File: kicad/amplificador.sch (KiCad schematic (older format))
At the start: 77 parts, among them J1 Screw_Terminal_01x01, J10 Conn_01x01_Male, J11 Conn_01x01_Male, J12 Conn_01x01_Male, J13 Conn_01x01_Male, J14 Conn_01x01_Male, J15 Conn_01x01_Male, J16 Screw_Terminal_01x01, J17 Screw_Terminal_01x01, J18 Conn_01x01_Male, J2 Conn_01x01_Male, J3 Conn_01x01_Male, J4 Conn_01x01_Male, J5 Conn_01x01_Male, J6 Conn_01x01_Male, J7 Screw_Terminal_01x01, J8 Screw_Terminal_01x01, J9 Conn_01x01_Male, Q1 MPSA92, Q10 MPSA42, Q11 BD135, Q12 BD136, Q13 BD135, Q14 BD136, Q15 2SD1047, Q16 2SD1047, Q17 2SB817, Q18 2SB817, Q2 MPSA42, Q3 MPSA92, Q4 MPSA42, Q5 MPSA92, Q6 MPSA92, Q7 MPSA42, Q8 MPSA92, Q9 MPSA42, U1 LM385D-1.2, U2 LM385D-1.2

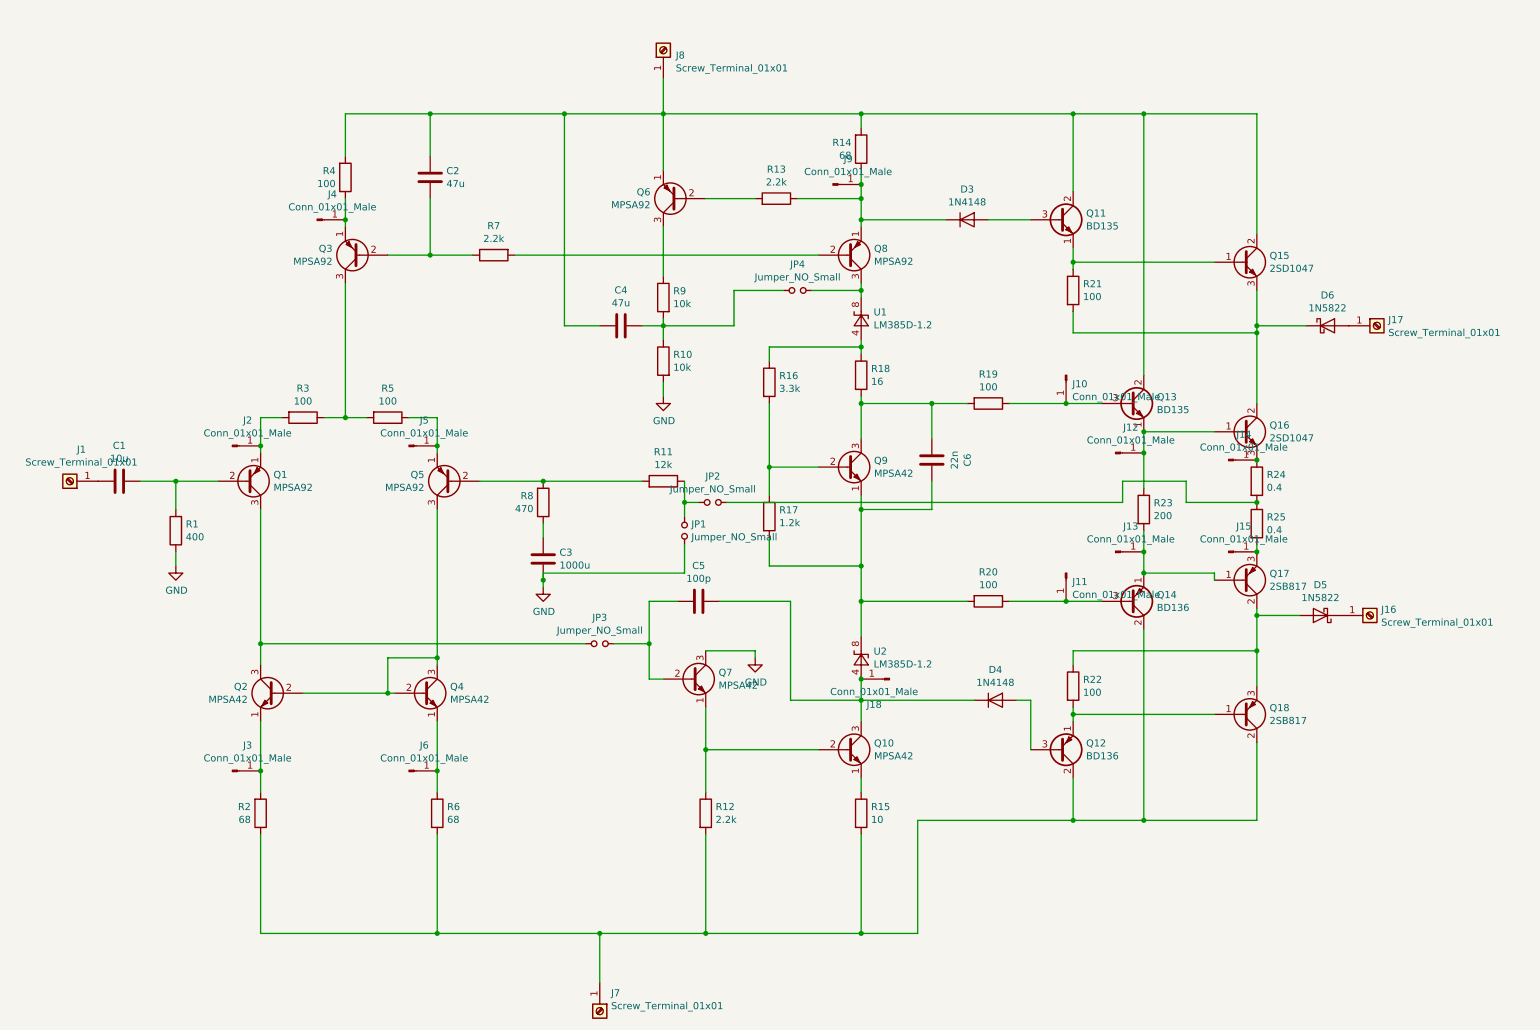
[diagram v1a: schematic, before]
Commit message: agregamos hojas de datos, cambiamos el esquematico un poco (footprints, sacamos algunos pines, agregamos capas de filtrado), el pcb esta dispuesto de la misma forma que el esquematico, queda optimizarlo y rutear
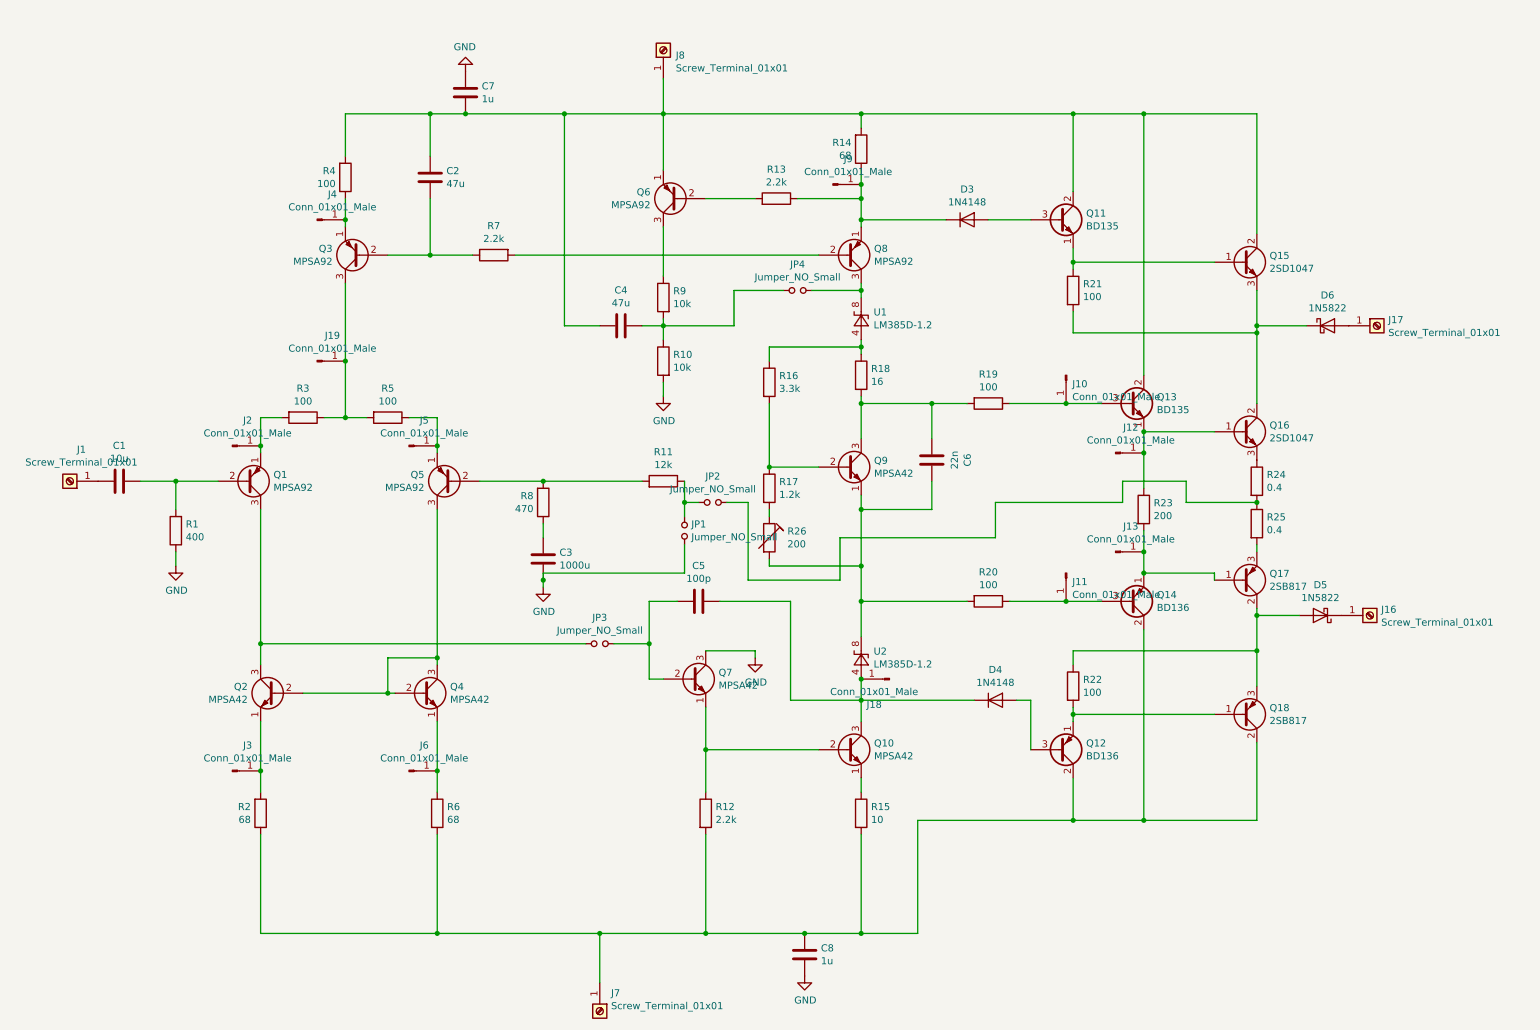
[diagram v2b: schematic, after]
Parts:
- removed J14, J15: Conn_01x01_Male, Connector_Pin:Pin_D0.7mm_L6.5mm_W1.8mm_FlatFork, symbol Connector:Conn_01x01_Male
- added C7, C8: 1u, Capacitor_THT:CP_Radial_D5.0mm_P2.00mm, symbol Device:C
- added J19: Conn_01x01_Male, Connector_Pin:Pin_D0.7mm_L6.5mm_W1.8mm_FlatFork, symbol Connector:Conn_01x01_Male
- added R26: 200, Resistor_THT:R_Box_L8.4mm_W2.5mm_P5.08mm, symbol Device:RTRIM
- R24, R25: footprint Resistor_SMD:R_0805_2012Metric_Pad1.15x1.40mm_HandSolder -> Resistor_THT:R_Axial_DIN0414_L11.9mm_D4.5mm_P25.40mm_Horizontal
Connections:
- net GND: now also C7.1, C8.2
- net at Q3.3 (C), R3.1, R5.2: now also J19.1 (Pin_1)
- net at J7.1 (Pin_1), Q12.2 (C), Q14.2 (C)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: now also C8.1
- net at C2.2, C4.2, J8.1 (Pin_1)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: now also C7.2
- net at C6.1, Q9.1 (E), R20.2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: now also R26.2; no longer R17.2
- new net: R17.2, R26.1
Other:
- moved on the sheet: R17
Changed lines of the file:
@@
 Connection ~ 5350 7050
 Wire Wire Line
-	5350 7050 6450 7050
+	5350 7050 6050 7050
 Wire Wire Line
 	3450 4050 3450 5100
@@
 	5050 2750 5050 2700
 Wire Wire Line
-	2800 2450 2800 3400
+	2800 2450 2800 3000
 Connection ~ 2800 3400
 Wire Wire Line
@@
 	5050 1000 5050 1250
 Wire Wire Line
-	3400 1250 4350 1250
+	3400 1250 3650 1250
 Wire Wire Line
 	4600 2750 4350 2750
@@
 L Device:R R17
 U 1 1 5D084E8F
-P 5800 4100
-F 0 "R17" H 5870 4146 50  0000 L CNN
-F 1 "1.2k" H 5870 4055 50  0000 L CNN
-F 2 "Resistor_SMD:R_0805_2012Metric_Pad1.15x1.40mm_HandSolder" V 5730 4100 50  0001 C CNN
-F 3 "~" H 5800 4100 50  0001 C CNN
-	1    5800 4100
+P 5800 3900
+F 0 "R17" H 5870 3946 50  0000 L CNN
+F 1 "1.2k" H 5870 3855 50  0000 L CNN
+F 2 "Resistor_SMD:R_0805_2012Metric_Pad1.15x1.40mm_HandSolder" V 5730 3900 50  0001 C CNN
+F 3 "~" H 5800 3900 50  0001 C CNN
+	1    5800 3900
 	1    0    0    -1
 $EndComp
@@
 Wire Wire Line
 	5800 2900 5800 3000
-Wire Wire Line
-	5800 3300 5800 3750
 Connection ~ 5800 3750
-Wire Wire Line
-	5800 3750 5800 3950
-Wire Wire Line
-	5800 4250 5800 4450
 Wire Wire Line
 	5800 4450 6450 4450
@@
 F 0 "R25" H 9320 4196 50  0000 L CNN
 F 1 "0.4" H 9320 4105 50  0000 L CNN
-F 2 "Resistor_SMD:R_0805_2012Metric_Pad1.15x1.40mm_HandSolder" V 9180 4150 50  0001 C CNN
+F 2 "Resistor_THT:R_Axial_DIN0414_L11.9mm_D4.5mm_P25.40mm_Horizontal" V 9180 4150 50  0001 C CNN
 F 3 "~" H 9250 4150 50  0001 C CNN
 	1    9250 4150
@@
 F 0 "R24" H 9320 3896 50  0000 L CNN
 F 1 "0.4" H 9320 3805 50  0000 L CNN
-F 2 "Resistor_SMD:R_0805_2012Metric_Pad1.15x1.40mm_HandSolder" V 9180 3850 50  0001 C CNN
+F 2 "Resistor_THT:R_Axial_DIN0414_L11.9mm_D4.5mm_P25.40mm_Horizontal" V 9180 3850 50  0001 C CNN
 F 3 "~" H 9250 3850 50  0001 C CNN
 	1    9250 3850
@@
 Wire Wire Line
 	8750 4000 9250 4000
-Wire Wire Line
-	5500 4000 8300 4000
 Connection ~ 9250 4000
 Wire Wire Line
@@
 	6450 1750 6450 1850
 $Comp
-L Connector:Conn_01x01_Male J14
-U 1 1 5D20277F
-P 9050 3700
-F 0 "J14" H 9158 3881 50  0000 C CNN
-F 1 "Conn_01x01_Male" H 9158 3790 50  0000 C CNN
-F 2 "Connector_Pin:Pin_D0.7mm_L6.5mm_W1.8mm_FlatFork" H 9050 3700 50  0001 C CNN
-F 3 "~" H 9050 3700 50  0001 C CNN
-	1    9050 3700
-	1    0    0    -1
-$EndComp
-Connection ~ 9250 3700
-$Comp
-L Connector:Conn_01x01_Male J15
-U 1 1 5D20324F
-P 9050 4350
-F 0 "J15" H 9158 4531 50  0000 C CNN
-F 1 "Conn_01x01_Male" H 9158 4440 50  0000 C CNN
-F 2 "Connector_Pin:Pin_D0.7mm_L6.5mm_W1.8mm_FlatFork" H 9050 4350 50  0001 C CNN
-F 3 "~" H 9050 4350 50  0001 C CNN
-	1    9050 4350
-	1    0    0    -1
-$EndComp
-$Comp
 L Connector:Conn_01x01_Male J10
 U 1 1 5D20366F
@@
 Wire Wire Line
 	9250 4350 9250 4300
-Connection ~ 9250 4350
 Wire Wire Line
 	5950 5400 6450 5400
@@
 Wire Wire Line
 	5550 2750 5050 2750
+$Comp
+L Connector:Conn_01x01_Male J19
+U 1 1 5D204C85
+P 2600 3000
+F 0 "J19" H 2708 3181 50  0000 C CNN
+F 1 "Conn_01x01_Male" H 2708 3090 50  0000 C CNN
+F 2 "Connector_Pin:Pin_D0.7mm_L6.5mm_W1.8mm_FlatFork" H 2600 3000 50  0001 C CNN
+F 3 "~" H 2600 3000 50  0001 C CNN
+	1    2600 3000
+	1    0    0    -1
+$EndComp
+Connection ~ 2800 3000
+Wire Wire Line
+	2800 3000 2800 3400
+Wire Wire Line
+	5800 4050 5800 4100
+Wire Wire Line
+	5800 3300 5800 3750
+Wire Wire Line
+	5800 4400 5800 4450
+$Comp
+L Device:RTRIM R26
+U 1 1 5D251E27
+P 5800 4250
+F 0 "R26" H 5928 4296 50  0000 L CNN
+F 1 "200" H 5928 4205 50  0000 L CNN
+F 2 "Resistor_THT:R_Box_L8.4mm_W2.5mm_P5.08mm" V 5730 4250 50  0001 C CNN
+F 3 "~" H 5800 4250 50  0001 C CNN
+	1    5800 4250
+	1    0    0    -1
+$EndComp
+Wire Wire Line
+	8300 4000 7400 4000
+Wire Wire Line
+	7400 4000 7400 4250
+Wire Wire Line
+	7400 4250 6300 4250
+Wire Wire Line
+	6300 4250 6300 4550
+Wire Wire Line
+	6300 4550 5650 4550
+Wire Wire Line
+	5650 4550 5650 4000
+Wire Wire Line
+	5650 4000 5500 4000
+$Comp
+L Device:C C8
+U 1 1 5D2CF0A1
+P 6050 7200
+F 0 "C8" H 6165 7246 50  0000 L CNN
+F 1 "1u" H 6165 7155 50  0000 L CNN
+F 2 "Capacitor_THT:CP_Radial_D5.0mm_P2.00mm" H 6088 7050 50  0001 C CNN
+F 3 "~" H 6050 7200 50  0001 C CNN
+	1    6050 7200
+	1    0    0    -1
+$EndComp
+Connection ~ 6050 7050
+Wire Wire Line
+	6050 7050 6450 7050
+$Comp
+L power:GND #PWR04
+U 1 1 5D2CFEDE
+P 6050 7350
+F 0 "#PWR04" H 6050 7100 50  0001 C CNN
+F 1 "GND" H 6055 7177 50  0000 C CNN
+F 2 "" H 6050 7350 50  0001 C CNN
+F 3 "" H 6050 7350 50  0001 C CNN
+	1    6050 7350
+	1    0    0    -1
+$EndComp
+$Comp
+L Device:C C7
+U 1 1 5D2D03B4
+P 3650 1100
+F 0 "C7" H 3765 1146 50  0000 L CNN
+F 1 "1u" H 3765 1055 50  0000 L CNN
+F 2 "Capacitor_THT:CP_Radial_D5.0mm_P2.00mm" H 3688 950 50  0001 C CNN
+F 3 "~" H 3650 1100 50  0001 C CNN
+	1    3650 1100
+	1    0    0    -1
+$EndComp
+Connection ~ 3650 1250
+Wire Wire Line
+	3650 1250 4350 1250
+$Comp
+L power:GND #PWR03
+U 1 1 5D2D9DE0
+P 3650 950
+F 0 "#PWR03" H 3650 700 50  0001 C CNN
+F 1 "GND" H 3655 777 50  0000 C CNN
+F 2 "" H 3650 950 50  0001 C CNN
+F 3 "" H 3650 950 50  0001 C CNN
+	1    3650 950
+	-1   0    0    1
+$EndComp
 $EndSCHEMATC

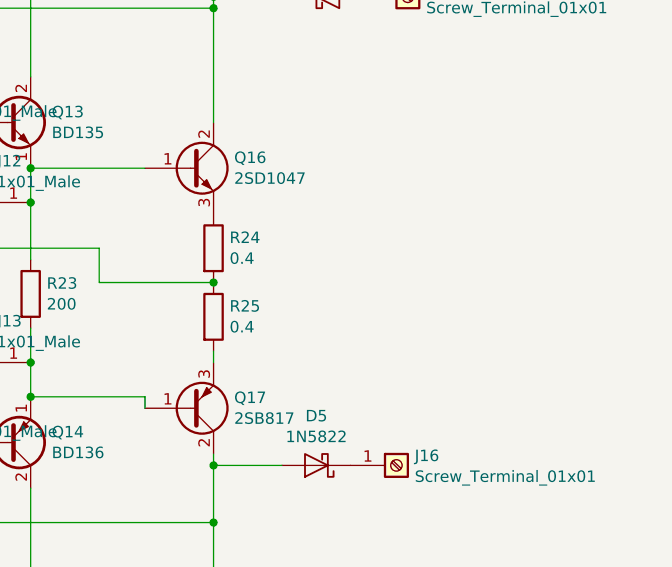
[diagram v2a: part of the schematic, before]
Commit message: PCB DRC actualizado
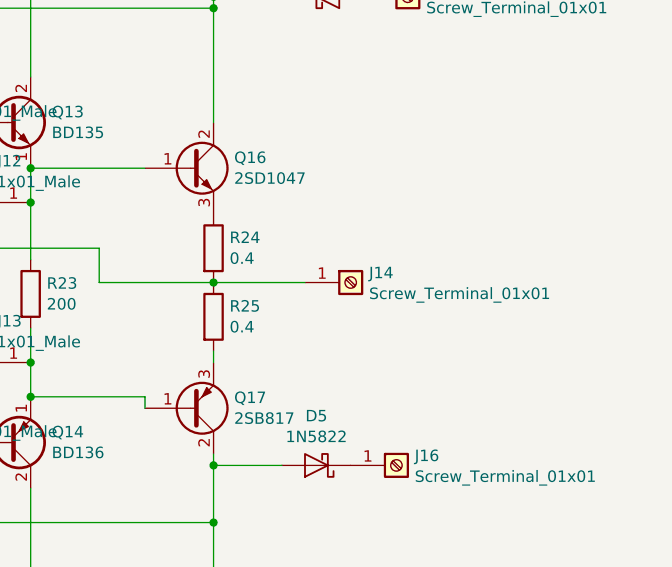
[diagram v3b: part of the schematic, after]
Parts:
- added J14: Screw_Terminal_01x01, Connector_Wire:SolderWirePad_1x01_Drill0.8mm, symbol Connector:Screw_Terminal_01x01
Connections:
- net at JP2.2, R24.2, R25.1: now also J14.1 (Pin_1)
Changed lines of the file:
@@
 	-1   0    0    1
 $EndComp
+$Comp
+L Connector:Screw_Terminal_01x01 J14
+U 1 1 5D20D458
+P 9850 4000
+F 0 "J14" H 9930 4042 50  0000 L CNN
+F 1 "Screw_Terminal_01x01" H 9930 3951 50  0000 L CNN
+F 2 "Connector_Wire:SolderWirePad_1x01_Drill0.8mm" H 9850 4000 50  0001 C CNN
+F 3 "~" H 9850 4000 50  0001 C CNN
+	1    9850 4000
+	1    0    0    -1
+$EndComp
+Wire Wire Line
+	9650 4000 9250 4000
 $EndSCHEMATC
